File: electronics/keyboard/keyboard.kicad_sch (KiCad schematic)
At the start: 87 parts, among them J0 Conn_01x04_Socket, SW0 `~, SW1 Esc, SW10 S, SW11 Z, SW12 3#, SW13 E, SW14 D, SW15 X, SW16 4$, SW17 R, SW18 F, SW19 C, SW2 Tab, SW20 5%, SW21 T, SW22 G, SW23 V, SW24 6^, SW25 Y, SW26 H, SW27 B, SW28 7&, SW29 U, SW3 Shift, SW30 J, SW31 N, SW32 8*, SW33 I, SW34 K, SW35 M, SW36 Boot, SW37 9(, SW38 O, SW39 L, SW4 1!, SW40 ,<, SW41 0), SW42 P, SW43 ;:, SW44 .>, SW45 -_, SW46 [{, SW47 '", SW48 /?, SW49 =+, SW5 Q, SW50 ]}, SW51 Enter, SW52 Space, SW53 Back, SW54 \|, SW55 Ctrl, SW56 Alt, SW57 Up, SW58 Down, SW59 Left, SW6 A, SW60 Right, SW7 FN, SW8 2@, SW9 W, U0 NCP1117-3.3_SOT223, U1 RP2040, U2 W25Q128JVS, Y0 ABM8-272-T3

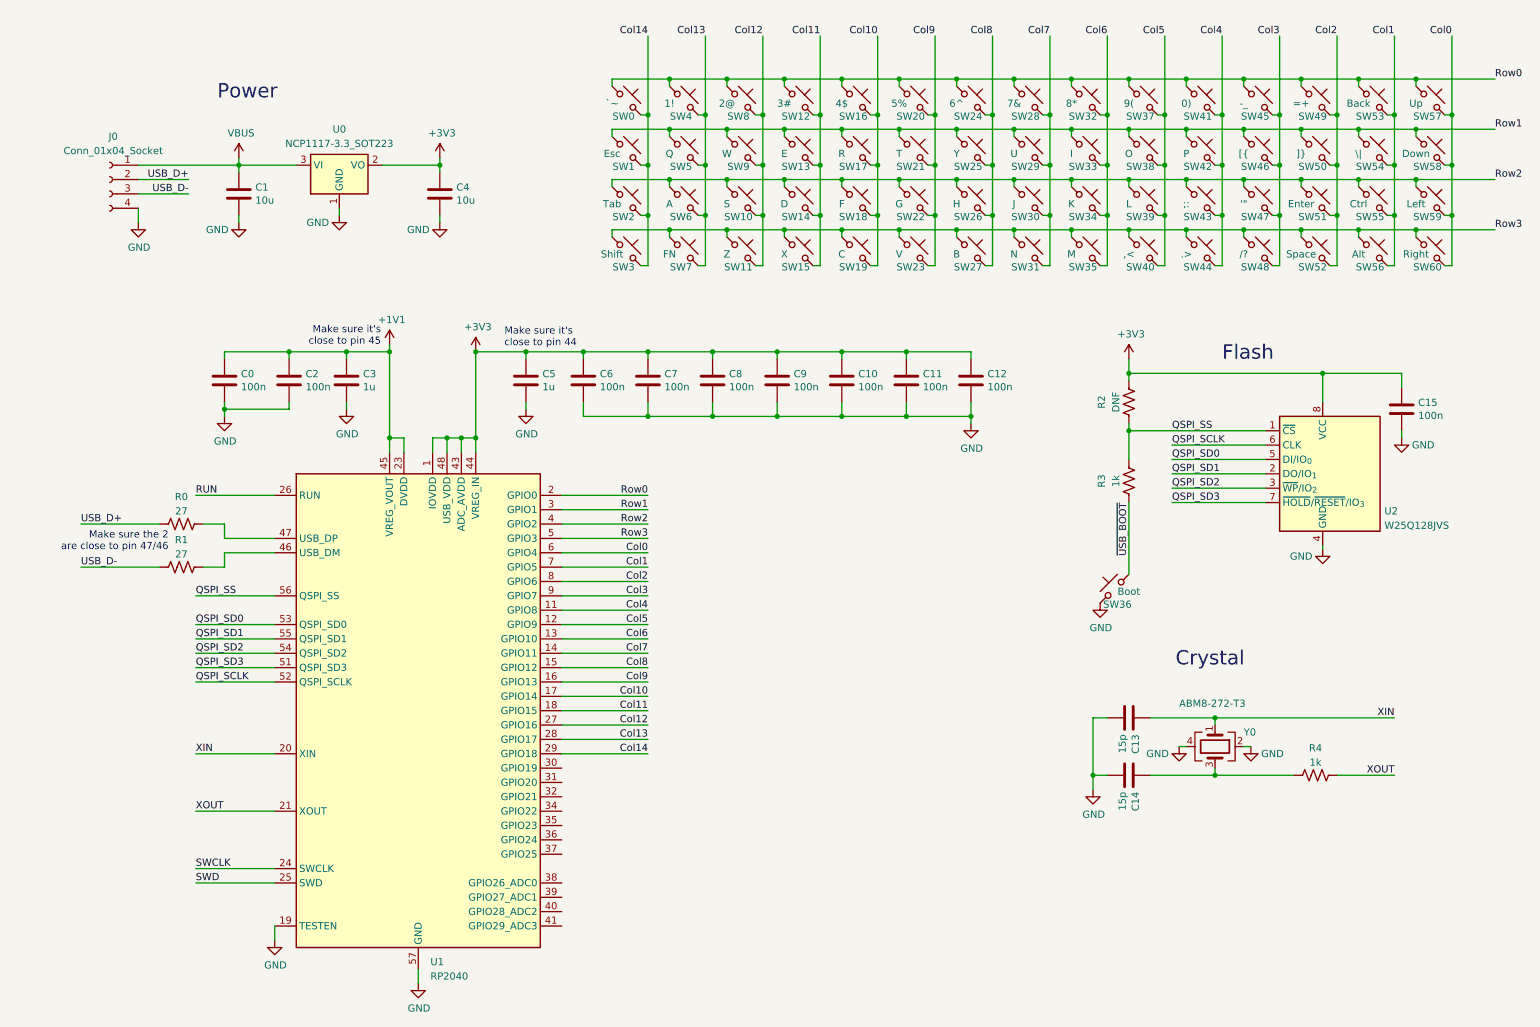
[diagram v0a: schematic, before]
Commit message: updating schematic of the keyboard
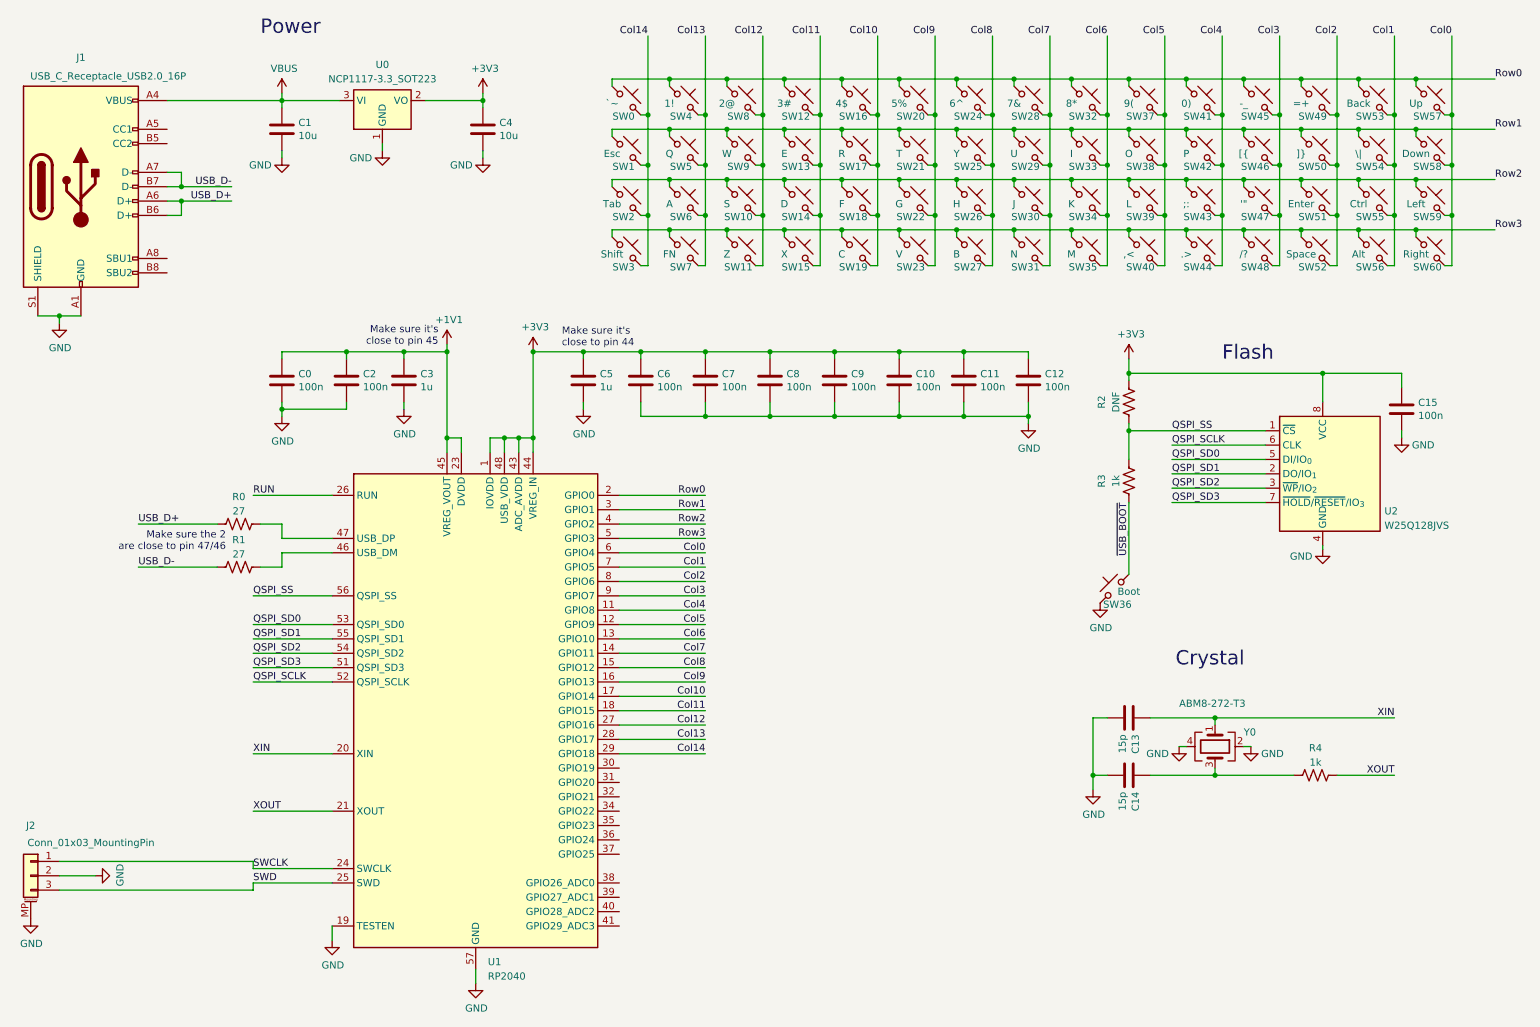
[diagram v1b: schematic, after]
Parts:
- removed J0: Conn_01x04_Socket, Connector_Molex:Molex_PicoBlade_53048-0410_1x04_P1.25mm_Horizontal, symbol Connector:Conn_01x04_Socket
- added J1: USB_C_Receptacle_USB2.0_16P, Connector_USB:USB_C_Receptacle_GCT_USB4085, symbol Connector:USB_C_Receptacle_USB2.0_16P
- added J2: Conn_01x03_MountingPin, Connector_JST:JST_SH_SM03B-SRSS-TB_1x03-1MP_P1.00mm_Horizontal, symbol Connector_Generic_MountingPin:Conn_01x03_MountingPin
- SW0, SW1, SW10, SW11, SW12, SW13, SW14, SW15, SW16, SW17, SW18, SW19, SW2, SW20, SW21, SW22, SW23, SW24, SW25, SW26, SW27, SW28, SW29, SW3, SW30, SW31, SW32, SW33, SW34, SW35, SW36, SW37, SW38, SW39, SW4, SW40, SW41, SW42, SW43, SW44, SW45, SW46, SW47, SW48, SW49, SW5, SW50, SW51, SW52, SW53, SW54, SW55, SW56, SW57, SW58, SW59, SW6, SW60, SW7, SW8, SW9: footprint Button_Switch_SMD:SW_SPST_PTS647_Sx70 -> Button_Switch_THT:SW_PUSH_6mm_H9.5mm
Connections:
- net GND: now also J1.A1 (GND), J1.A12 (GND), J1.B1 (GND), J1.B12 (GND), J1.S1 (SHIELD), J2.2 (Pin_2), J2.MP (MountPin)
- net SWCLK: now also J2.1 (Pin_1)
- net SWD: now also J2.3 (Pin_3)
- net USB_D+: now also J1.A6 (D+), J1.B6 (D+)
- net USB_D-: now also J1.A7 (D-), J1.B7 (D-)
- net VBUS: now also J1.A4 (VBUS), J1.A9 (VBUS), J1.B4 (VBUS), J1.B9 (VBUS)
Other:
- moved on the sheet: C0, C1, C10, C11, C12, C2, C3, C4, C5, C6, C7, C8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
